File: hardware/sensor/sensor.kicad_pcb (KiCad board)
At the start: 2 copper layers, 1 part, among them IC1 ATTINY202-SSN

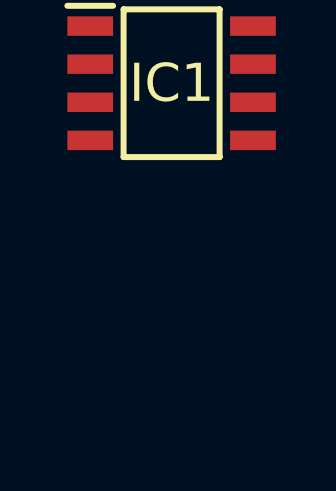
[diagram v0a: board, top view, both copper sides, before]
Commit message: EG-21 Added datasheets and the main ICs to KiCad project library, including symbol, footprint and 3D model.
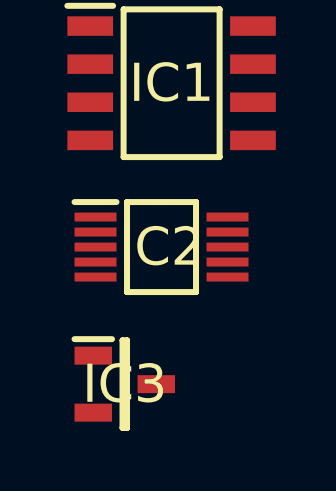
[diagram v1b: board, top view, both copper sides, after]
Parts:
- added IC2: Si4012-C1001GTR, MyParts:SOP50P490X110-10N, F.Cu at (33.8, 31.2)
- added IC3: TPS3839L30DBZR, MyParts:SOT95P237X112-3N, F.Cu at (32.6, 35.8)

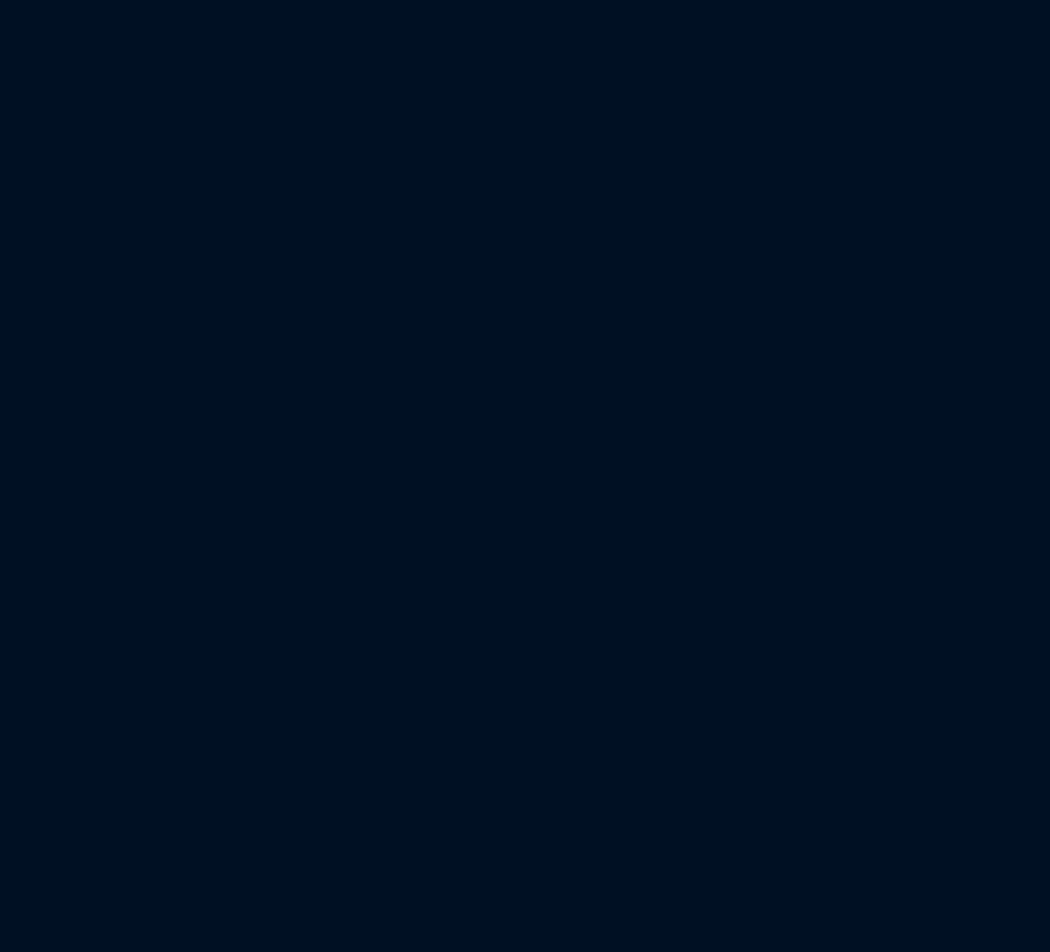
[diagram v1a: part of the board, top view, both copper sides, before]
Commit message: EG-21 Main components on schematic. Only missing I2C resistors, antenna, MCU RESET signal handling  and signals MCU<->Si4012.
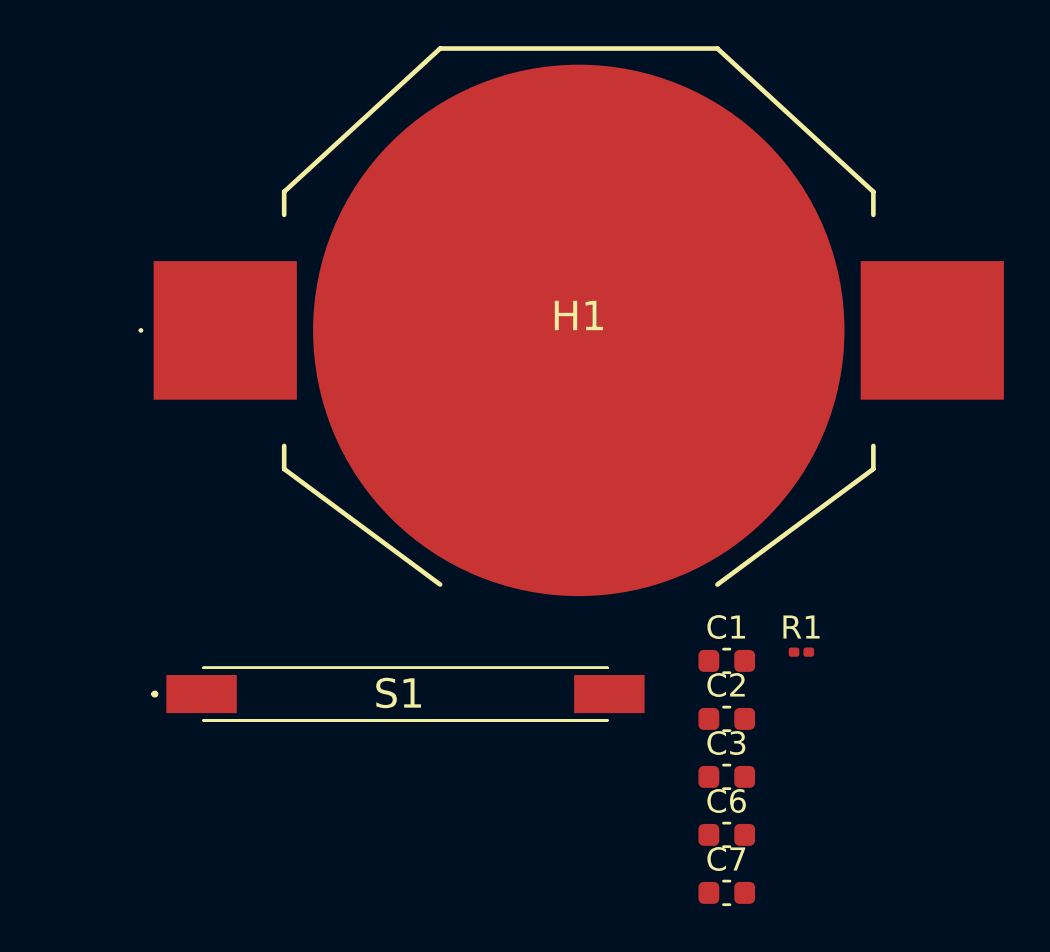
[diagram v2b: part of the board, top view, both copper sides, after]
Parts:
- added C1: 100 nF, Capacitor_SMD:C_0603_1608Metric, F.Cu at (85.8, 46.1)
- added C2: 100 nF, Capacitor_SMD:C_0603_1608Metric, F.Cu at (85.8, 48.6)
- added C3: 100 nF, Capacitor_SMD:C_0603_1608Metric, F.Cu at (85.8, 51.1)
- added C6: 1 uF, Capacitor_SMD:C_0603_1608Metric, F.Cu at (85.8, 53.6)
- added C7: 100 nF, Capacitor_SMD:C_0603_1608Metric, F.Cu at (85.8, 56.1)
- added H1: BAT-HLD-006-SMT, MyParts:BATHLD006SMT, F.Cu at (79.4, 31.8)
- added R1: 100K, Resistor_SMD:R_0201_0603Metric, F.Cu at (89.1, 45.7)
- added S1: MASM-14R-8-10, MyParts:MASM14R810, F.Cu at (71.9, 47.5)
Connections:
- IC1 pad 1: unconnected-(IC1-VDD-Pad1) -> 3.0 V
- IC1 pad 2: unconnected-(IC1-PA6-Pad2) -> LOW_BAT
- IC1 pad 3: unconnected-(IC1-PA7-Pad3) -> WND
- IC1 pad 8: unconnected-(IC1-GND-Pad8) -> GND
- IC2 pad 2: unconnected-(IC2-GND-Pad2) -> GND
- IC2 pad 5: unconnected-(IC2-VDD-Pad5) -> 3.0 V
- IC3 pad 1: unconnected-(IC3-GND-Pad1) -> GND
- IC3 pad 2: unconnected-(IC3-~{RESET}-Pad2) -> LOW_BAT
- IC3 pad 3: unconnected-(IC3-VDD-Pad3) -> 3.0 V

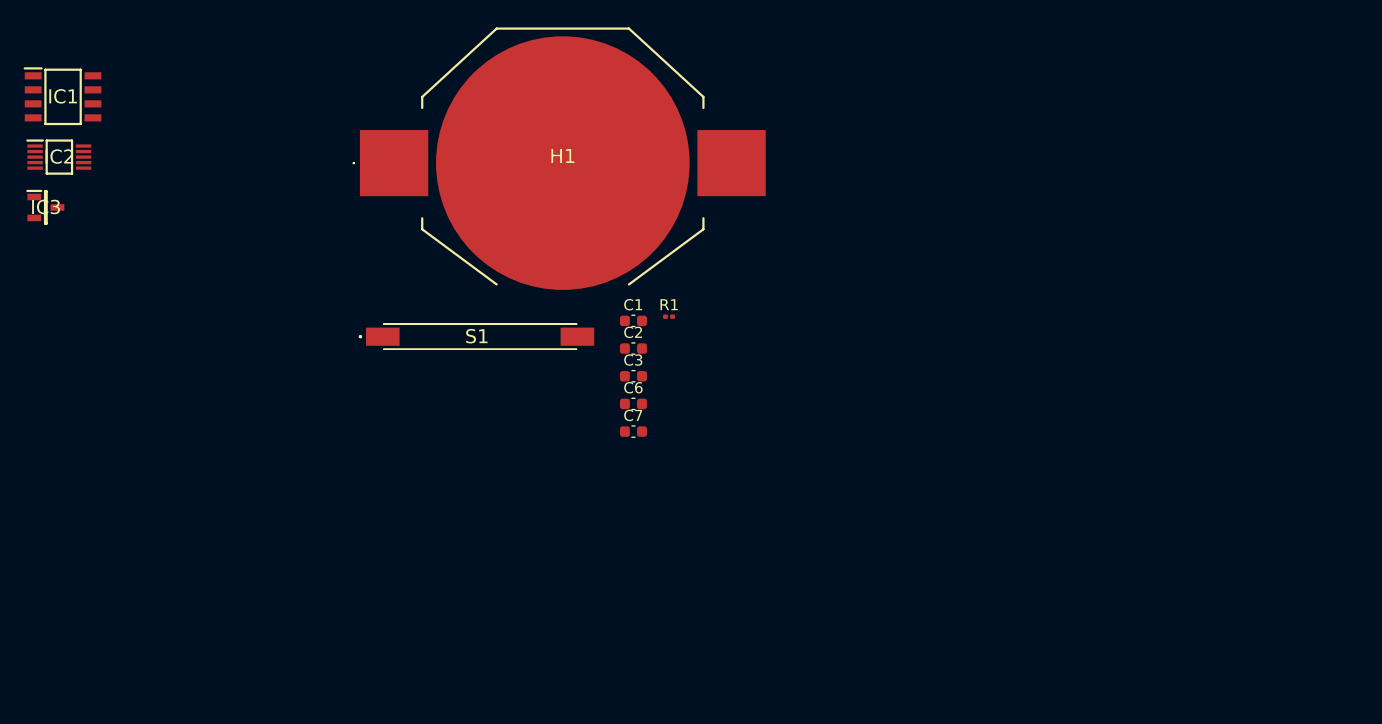
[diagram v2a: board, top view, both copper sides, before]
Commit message: EG-21 Antenna and programming headers added. Missing the balun part and test points.
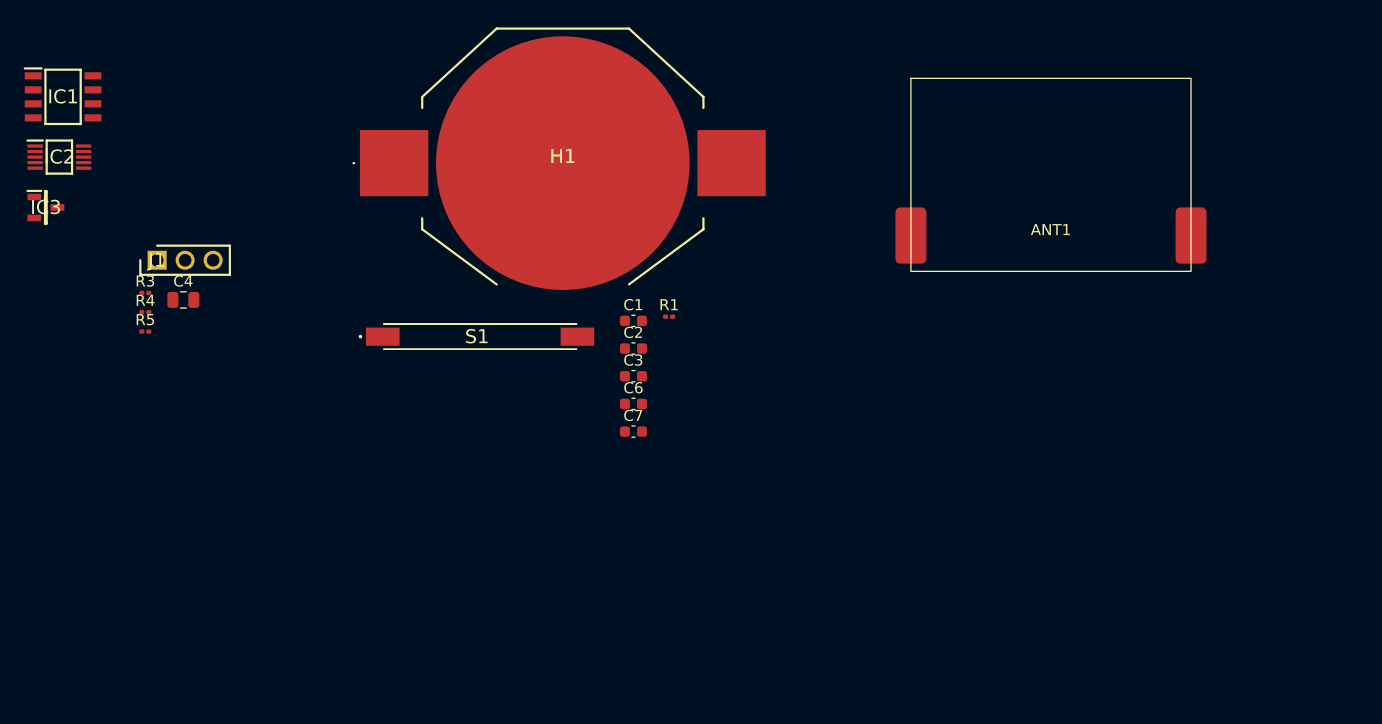
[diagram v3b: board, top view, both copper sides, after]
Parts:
- added ANT1: ANT-868-HETH, MyParts:ANT-868-HESM, F.Cu at (123.7, 38.4)
- added C4: 47uF, 6.3V, Capacitor_SMD:C_0805_2012Metric, F.Cu at (45.0, 44.2)
- added J1: M20-9770342, MyParts:HDRV3W66P0X254_1X3_762X254X855P, F.Cu at (42.6, 40.6)
- added R3: 100K, Resistor_SMD:R_0201_0603Metric, F.Cu at (41.6, 43.6)
- added R4: 10K, Resistor_SMD:R_0201_0603Metric, F.Cu at (41.6, 45.3)
- added R5: 10K, Resistor_SMD:R_0201_0603Metric, F.Cu at (41.6, 47.1)
- C1, C2, C3, C7: value 100 nF -> 100nF
- C6: value 1 uF -> 1uF
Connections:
- net 3.0 V renamed 3.0V
- IC1 pad 4: unconnected-(IC1-PA1-Pad4) -> SDN
- IC1 pad 5: unconnected-(IC1-PA2-Pad5) -> SDA
- IC1 pad 6: unconnected-(IC1-PA0/~{RESET}/UPDI-Pad6) -> UPDI
- IC1 pad 7: unconnected-(IC1-PA3/EXTCLK-Pad7) -> SCL
- IC2 pad 10: unconnected-(IC2-SDA-Pad10) -> SDA
- IC2 pad 3: unconnected-(IC2-TXM-Pad3) -> TXM
- IC2 pad 4: unconnected-(IC2-TXP-Pad4) -> TXP
- IC2 pad 8: unconnected-(IC2-SDN-Pad8) -> SDN
- IC2 pad 9: unconnected-(IC2-SCL-Pad9) -> SCL

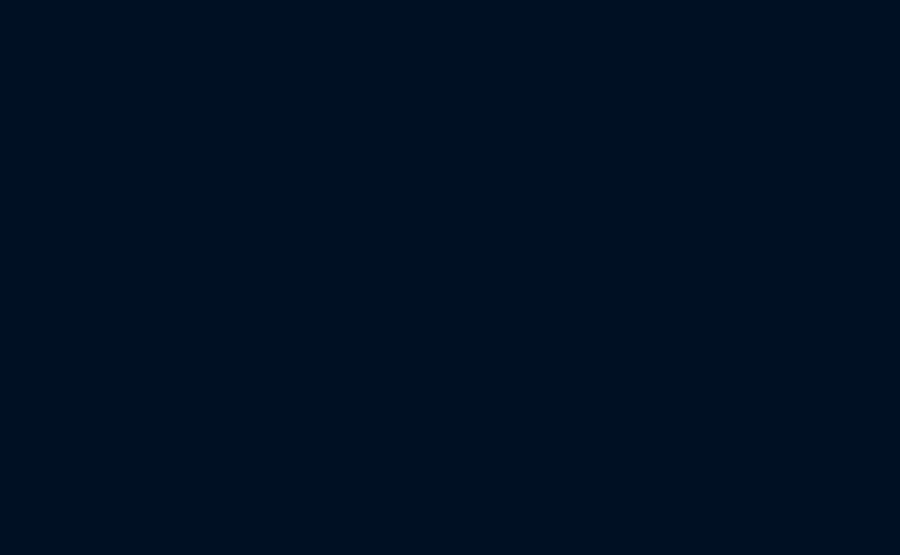
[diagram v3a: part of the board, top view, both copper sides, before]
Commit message: EG-21 Balun, pi-matching and antenna connected.
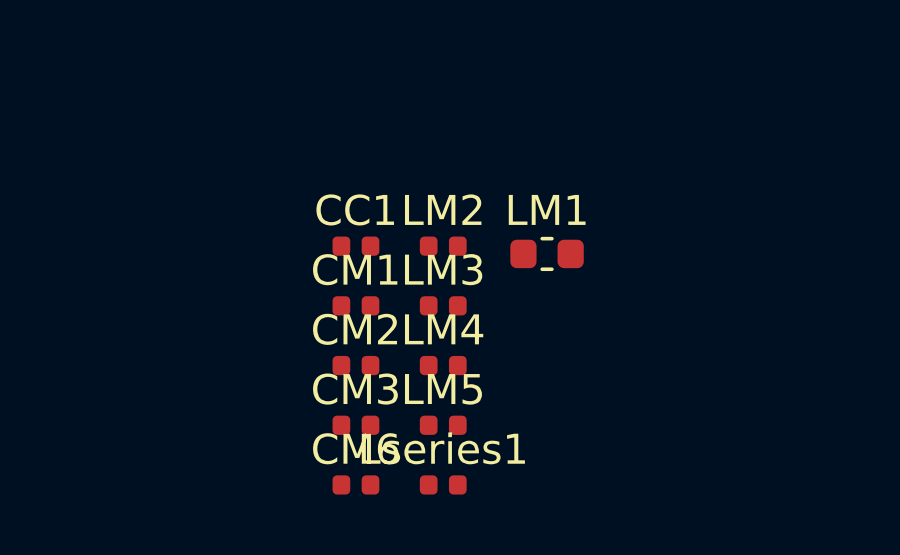
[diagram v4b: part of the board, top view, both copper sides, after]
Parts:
- added CC1: 68pF, Inductor_SMD:L_0402_1005Metric, F.Cu at (103.8, 50.5)
- added CM1: 2.4pF, Inductor_SMD:L_0402_1005Metric, F.Cu at (103.8, 52.5)
- added CM2: 1.2pF, Inductor_SMD:L_0402_1005Metric, F.Cu at (103.8, 54.4)
- added CM3: 2.4pF, Inductor_SMD:L_0402_1005Metric, F.Cu at (103.8, 56.4)
- added CM6: 5.1pF, Inductor_SMD:L_0402_1005Metric, F.Cu at (103.8, 58.4)
- added LM1: 120nH, Inductor_SMD:L_0603_1608Metric, F.Cu at (110.2, 50.7)
- added LM2: 3.6nH, Inductor_SMD:L_0402_1005Metric, F.Cu at (106.7, 50.5)
- added LM3: 30nH, Inductor_SMD:L_0402_1005Metric, F.Cu at (106.7, 52.5)
- added LM4: 3.6nH, Inductor_SMD:L_0402_1005Metric, F.Cu at (106.7, 54.4)
- added LM5: 6.8nH, Inductor_SMD:L_0402_1005Metric, F.Cu at (106.7, 56.4)
- added Lseries1: 15nH, Inductor_SMD:L_0402_1005Metric, F.Cu at (106.7, 58.4)
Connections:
- ANT1 pad 1: unconnected-(ANT1-Pad1) -> Net-(ANT1-Pad1)

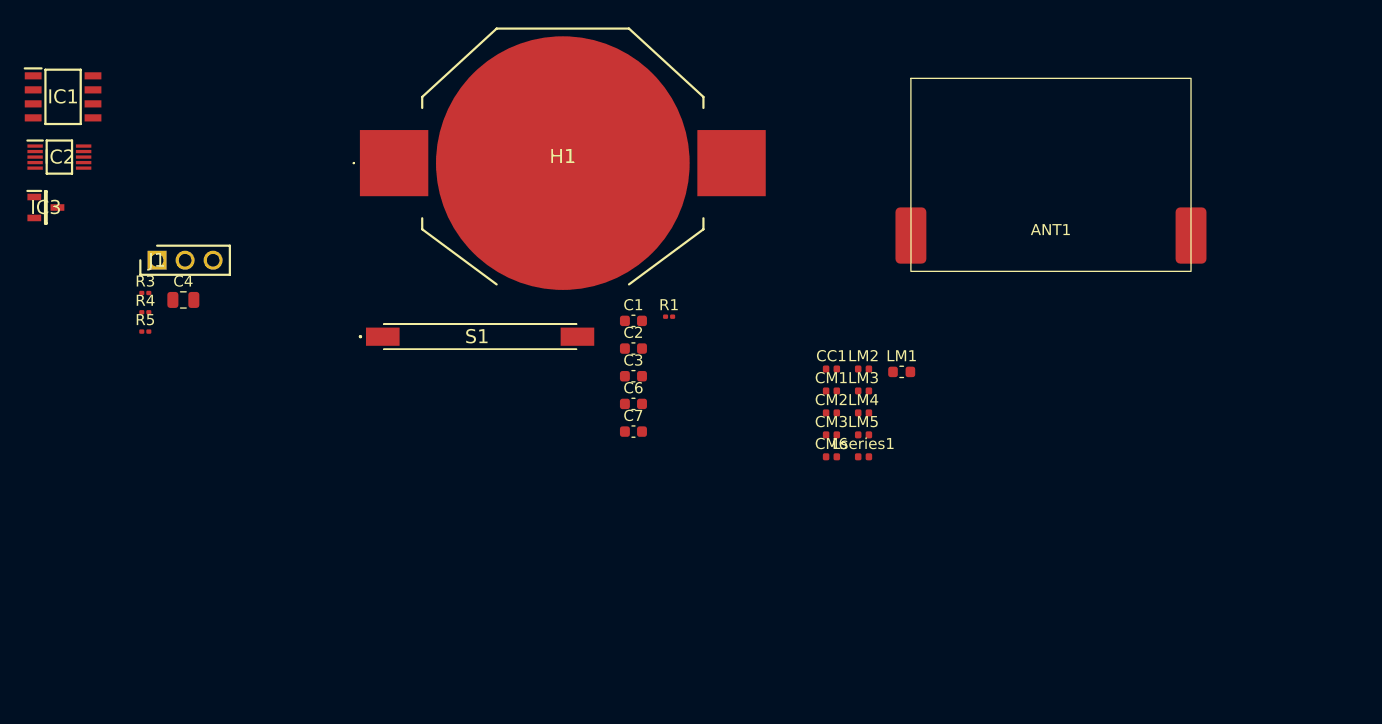
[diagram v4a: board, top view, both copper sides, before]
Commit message: EG-21 Schematic complete, without ERC errors. All components updated in the PCB.
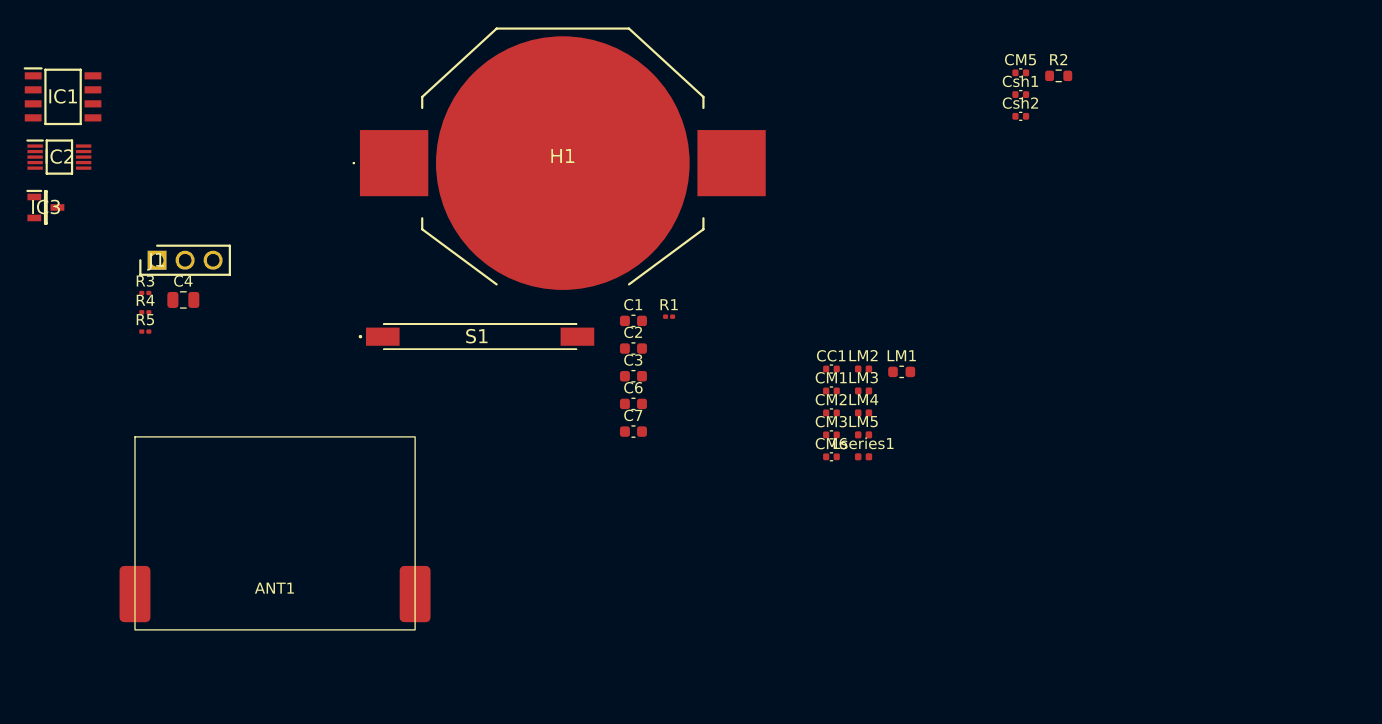
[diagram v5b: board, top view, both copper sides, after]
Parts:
- added CM5: 5.1pF, Capacitor_SMD:C_0402_1005Metric, F.Cu at (121.0, 23.6)
- added Csh1: 0pF, Capacitor_SMD:C_0402_1005Metric, F.Cu at (121.0, 25.6)
- added Csh2: 0pF, Capacitor_SMD:C_0402_1005Metric, F.Cu at (121.0, 27.5)
- added R2: 1M, Resistor_SMD:R_0603_1608Metric, F.Cu at (124.4, 23.9)
- ANT1: value ANT-868-HETH -> ANT-868-HESM
- CC1, CM1, CM2, CM3, CM6: footprint Inductor_SMD:L_0402_1005Metric -> Capacitor_SMD:C_0402_1005Metric
- moved ANT1 77.5 mm to (53.3, 70.9)
